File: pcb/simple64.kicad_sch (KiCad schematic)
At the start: 133 parts, among them J1 OLED Screen, SW1 Key, SW10 Key, SW11 Key, SW12 Key, SW13 Key, SW14 Key, SW15 Key, SW16 Key, SW17 Key, SW18 Key, SW19 Key, SW2 Key, SW20 Key, SW21 Key, SW22 Key, SW23 Key, SW24 Key, SW25 Key, SW26 Key, SW27 Key, SW28 Key, SW29 Key, SW3 Key, SW30 Key, SW31 Key, SW32 Key, SW33 Key, SW34 Key, SW35 Key, SW36 Key, SW37 Key, SW38 Key, SW39 Key, SW4 Key, SW40 Key, SW41 Key, SW42 Key, SW43 Key, SW44 Key, SW45 Key, SW46 Key, SW47 Key, SW48 Key, SW49 Key, SW5 Key, SW50 Key, SW51 Key, SW52 Key, SW53 Key, SW54 Key, SW55 Key, SW56 Key, SW57 Key, SW58 Key, SW59 Key, SW6 Key, SW60 Key, SW61 Key, SW62 Key, SW63 Key, SW64 Key, SW65 Key, SW66 RotaryEncoder_Switch, SW7 Key, SW8 Key, SW9 Key

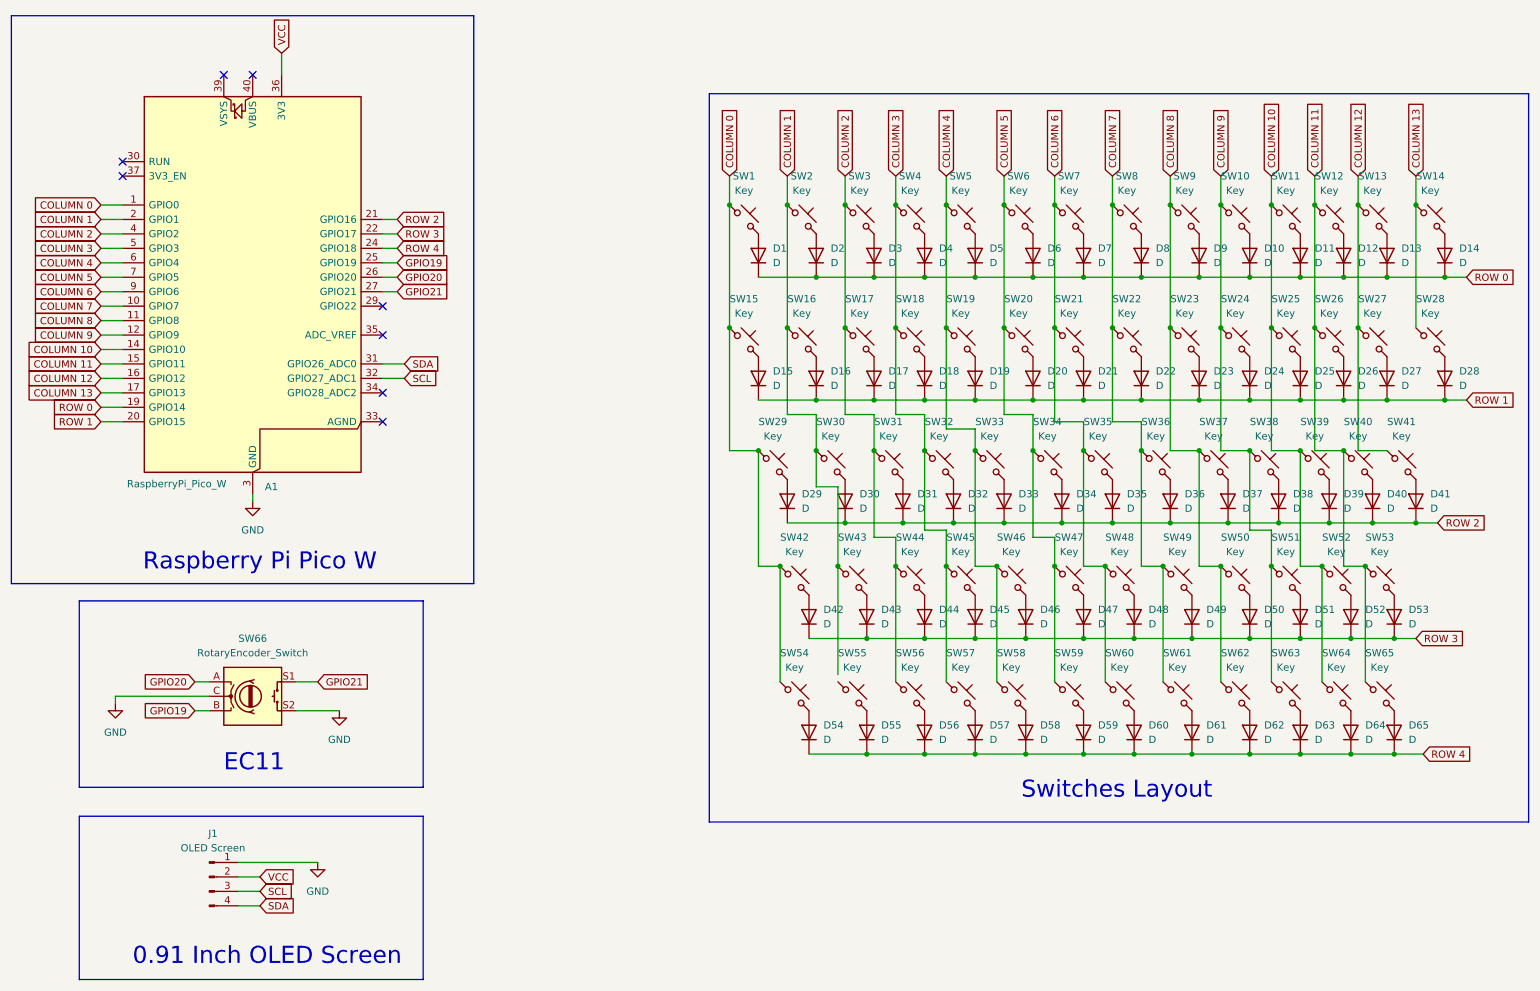
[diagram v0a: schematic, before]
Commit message: added the pcb, need to add mounting holes
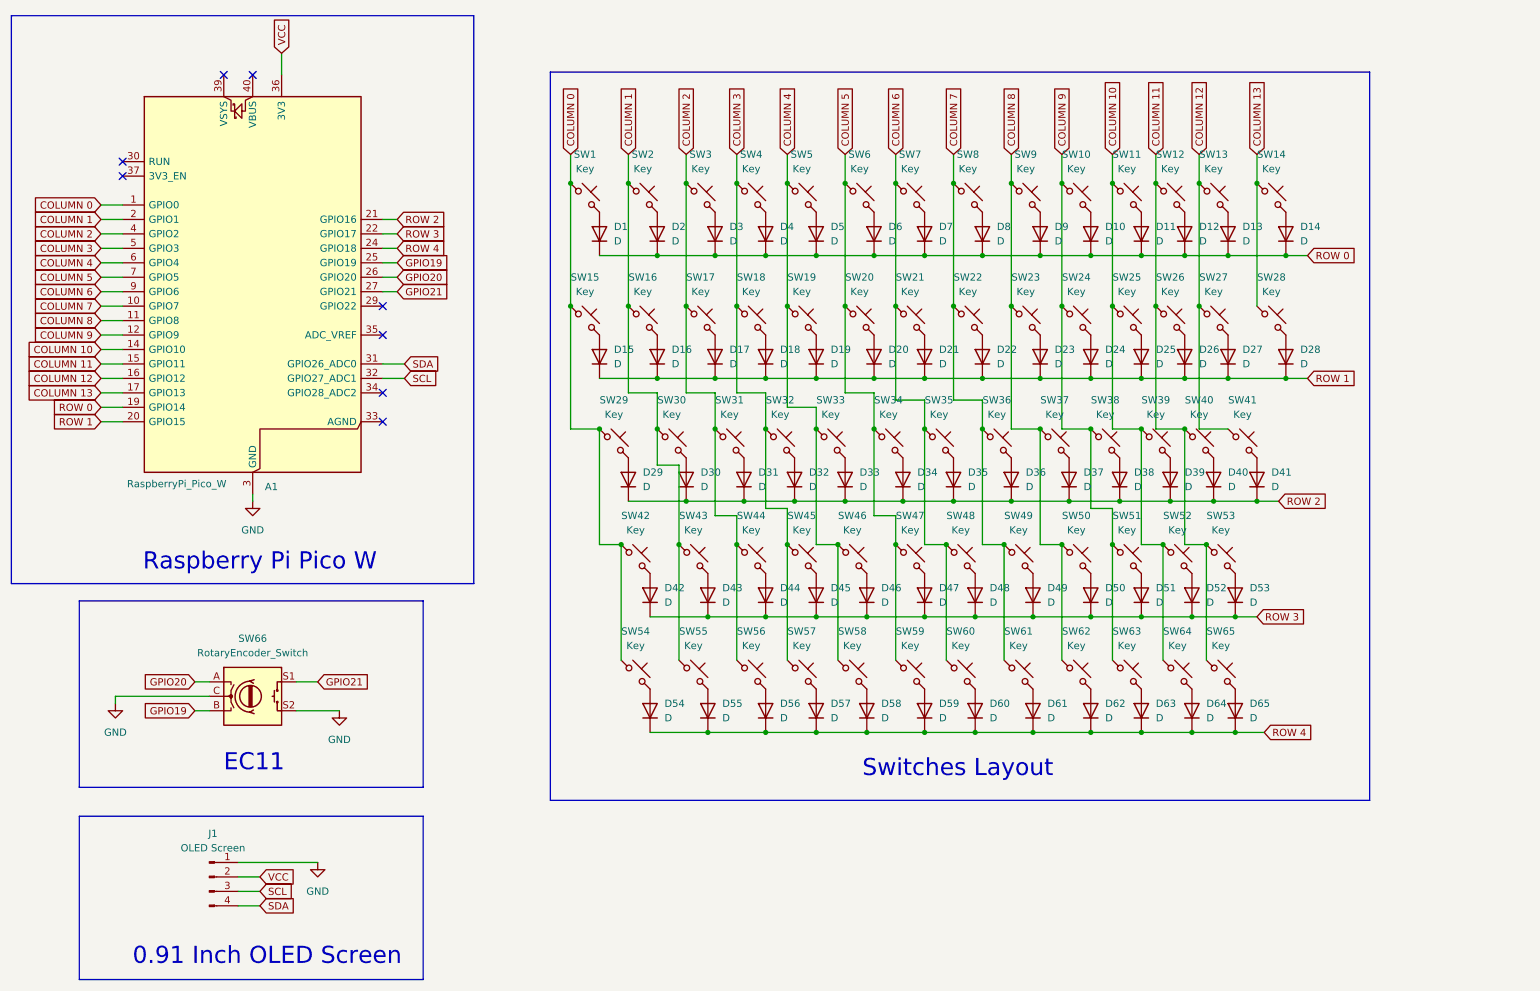
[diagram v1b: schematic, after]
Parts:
- A1: footprint Module:RaspberryPi_Pico_Common_THT -> 1N4148:MODULE_SC0918
- D1, D10, D11, D12, D13, D14, D15, D16, D17, D18, D19, D2, D20, D21, D22, D23, D24, D25, D26, D27, D28, D29, D3, D30, D31, D32, D33, D34, D35, D36, D37, D38, D39, D4, D40, D41, D42, D43, D44, D45, D46, D47, D48, D49, D5, D50, D51, D52, D53, D54, D55, D56, D57, D58, D59, D6, D60, D61, D62, D63, D64, D65, D7, D8, D9: footprint (none) -> 1N4148:Diode_DO-35
- J1: footprint (none) -> 1N4148:OLED_128x32
- SW1, SW10, SW11, SW12, SW13, SW14, SW15, SW16, SW17, SW18, SW19, SW2, SW20, SW21, SW22, SW23, SW24, SW25, SW26, SW27, SW28, SW29, SW3, SW30, SW31, SW32, SW33, SW34, SW35, SW36, SW37, SW38, SW39, SW4, SW40, SW41, SW42, SW43, SW44, SW45, SW46, SW47, SW48, SW49, SW5, SW50, SW51, SW52, SW53, SW54, SW55, SW56, SW57, SW58, SW59, SW6, SW60, SW61, SW62, SW63, SW64, SW65, SW7, SW8, SW9: footprint (none) -> Button_Switch_Keyboard:SW_Cherry_MX_1.00u_PCB
- SW66: footprint (none) -> Rotary_Encoder:RotaryEncoder_Alps_EC11E-Switch_Vertical_H20mm_CircularMountingHoles
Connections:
- net COLUMN 1: now also SW55.1
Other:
- moved on the sheet: D1, D10, D11, D12, D13, D14, D15, D16, D17, D18, D19, D2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
